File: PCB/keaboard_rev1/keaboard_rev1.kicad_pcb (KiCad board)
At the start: 2 copper layers, 136.5 x 87.7 mm, 100 parts, among them K01 KEYSW, K02 KEYSW, K03 KEYSW, K04 KEYSW, K05 KEYSW, K06 KEYSW, K07 KEYSW, K08 KEYSW, K09 KEYSW, K10 KEYSW, K11 KEYSW, K12 KEYSW, K13 KEYSW, K14 KEYSW, K15 KEYSW, K16 KEYSW, K17 KEYSW, K18 KEYSW, K19 KEYSW, K20 KEYSW, K21 KEYSW, K22 KEYSW, K23 KEYSW, K24 KEYSW, K25 KEYSW, U1 ProMicro

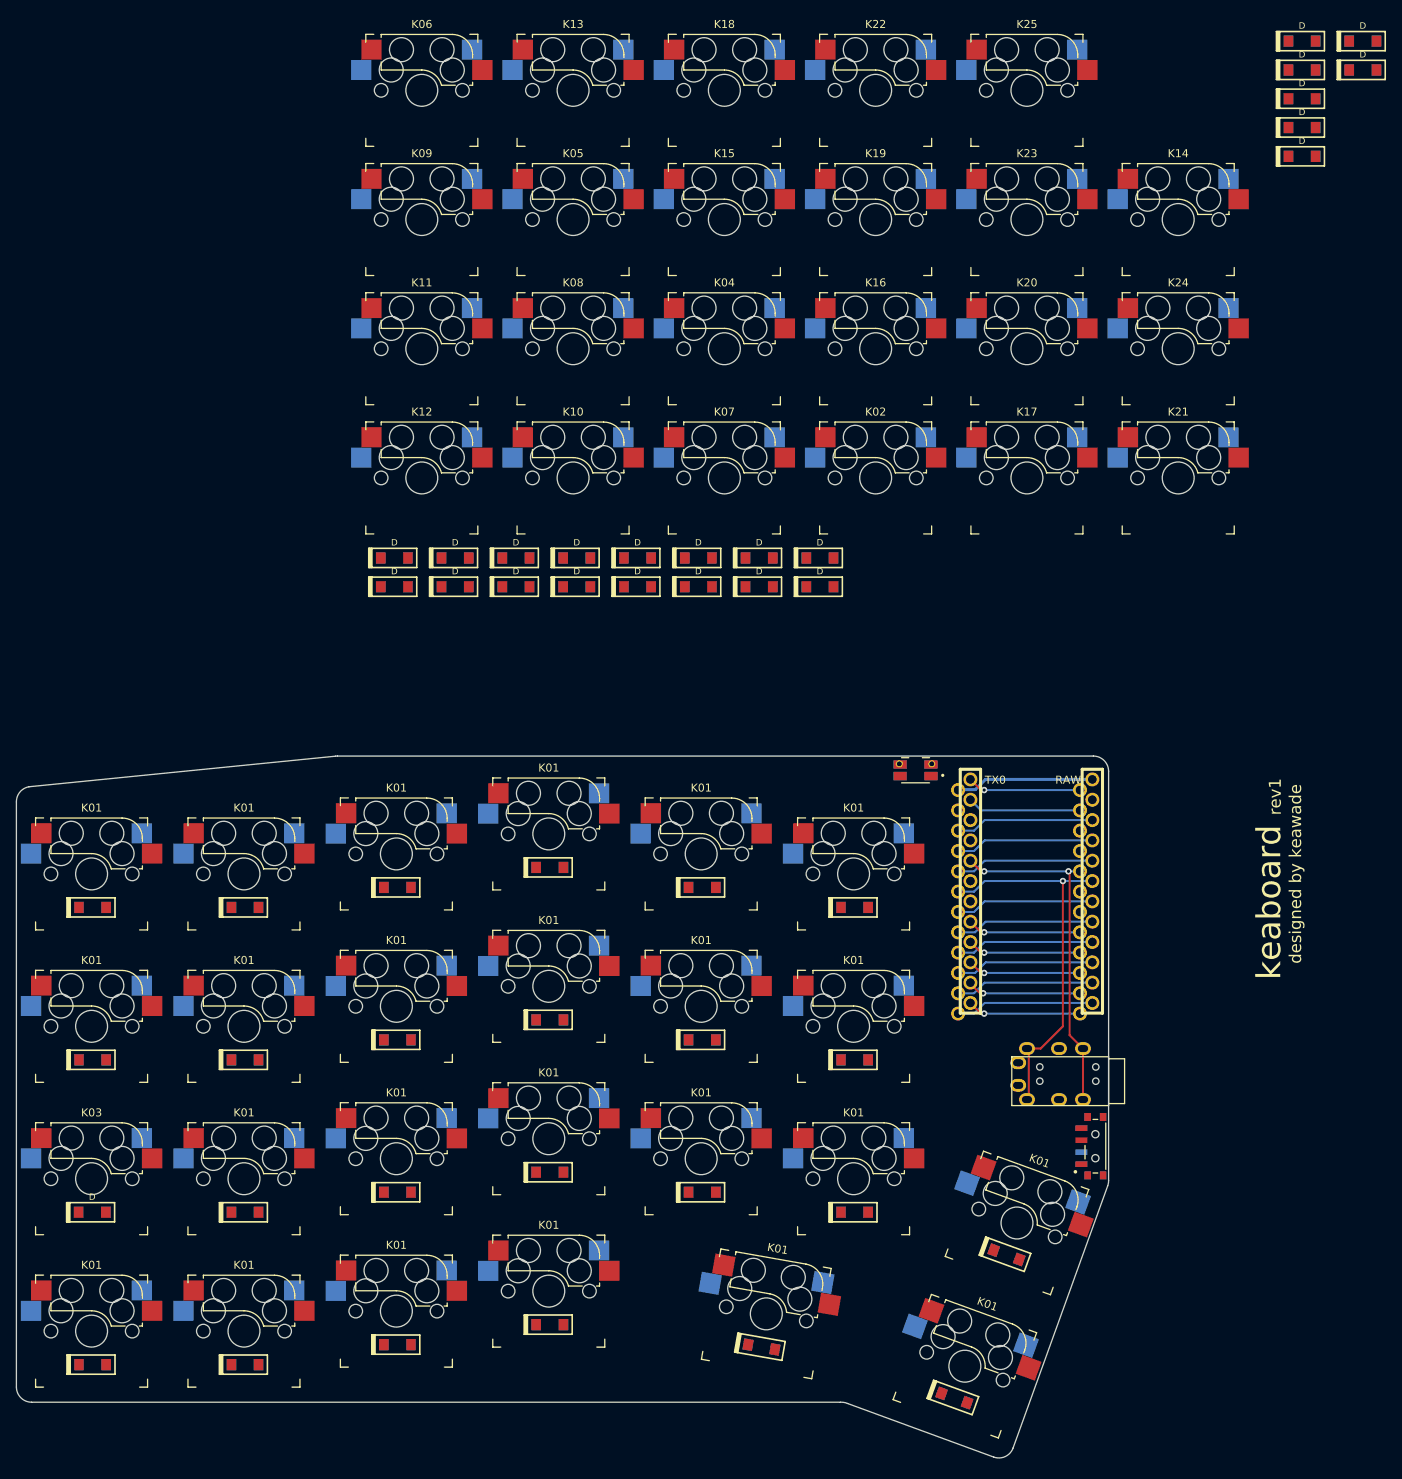
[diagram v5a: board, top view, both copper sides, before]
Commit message: Footprints laid out from schematic
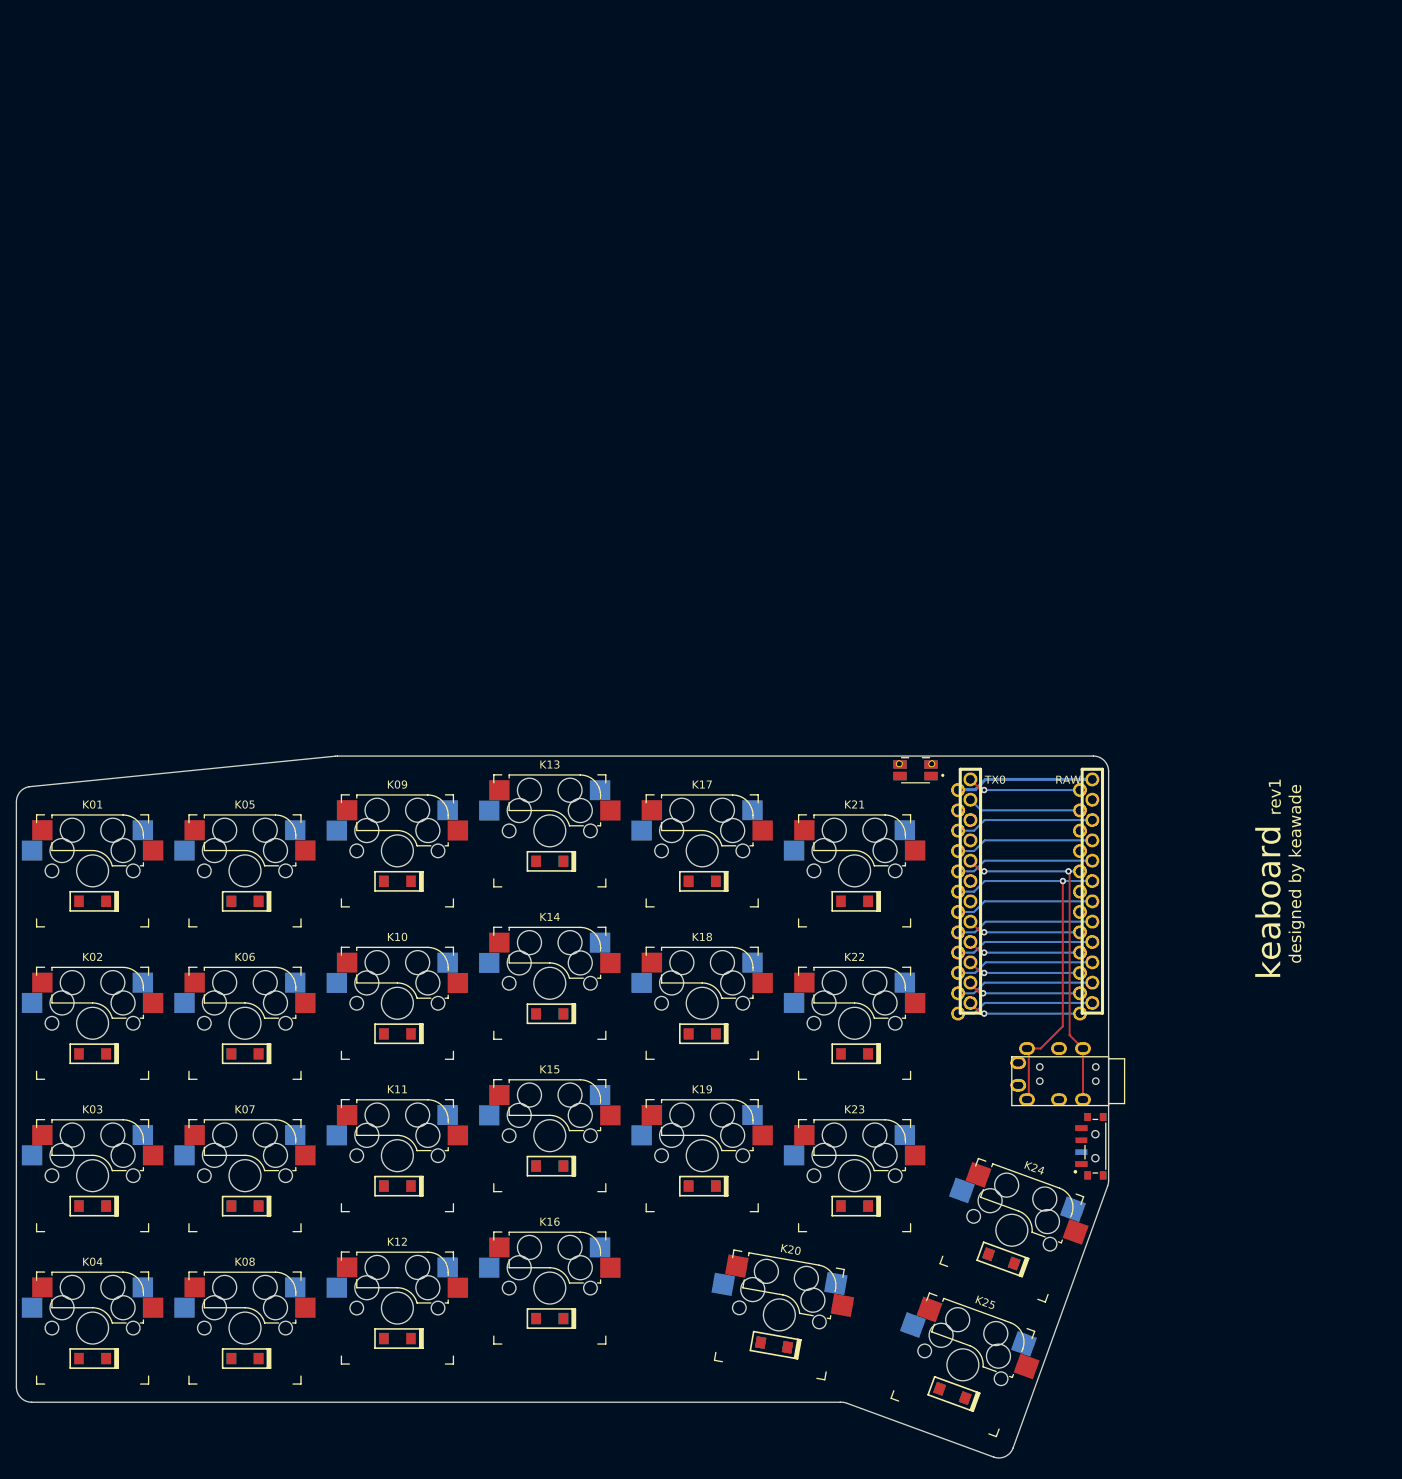
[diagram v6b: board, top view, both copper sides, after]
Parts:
- removed the D01 at (146.2, 107.9)
- removed the D01 at (95.6, 98.8)
- removed the D01 at (95.6, 79.7)
- removed the D01 at (95.6, 60.7)
- removed the D01 at (95.6, 41.6)
- removed the D01 at (76.6, 101.3)
- removed the D01 at (76.6, 82.2)
- removed the D01 at (76.6, 63.2)
- removed the D01 at (76.6, 44.1)
- removed the D01 at (57.5, 103.8)
- removed the D01 at (57.5, 84.7)
- removed the D01 at (152.7, 90.0)
- removed the D01 at (57.5, 65.7)
- removed the D01 at (57.5, 46.6)
- removed the D01 at (38.5, 103.8)
- removed the D01 at (38.5, 65.7)
- removed the D01 at (38.5, 46.6)
- removed the D01 at (122.1, 101.6)
- removed the D01 at (133.7, 84.7)
- removed the D01 at (133.7, 65.7)
- removed the D01 at (133.7, 46.6)
- removed the D01 at (114.7, 82.2)
- removed the D01 at (114.7, 63.2)
- removed the D01 at (114.7, 44.1)
- removed the K01 at (147.5, 104.0)
- removed the K01 at (95.5, 94.6)
- removed the K01 at (95.5, 75.5)
- removed the K01 at (95.5, 56.5)
- removed the K01 at (95.5, 37.4)
- removed the K01 at (76.5, 97.1)
- removed the K01 at (76.5, 78.0)
- removed the K01 at (76.5, 59.0)
- removed the K01 at (76.5, 39.9)
- removed the K01 at (57.4, 99.6)
- removed the K01 at (57.4, 80.5)
- removed the K01 at (154.0, 86.1)
- removed the K01 at (57.4, 61.5)
- removed the K01 at (57.4, 42.4)
- removed the K01 at (38.4, 99.6)
- removed the K01 at (38.4, 61.5)
- removed the K01 at (38.4, 42.4)
- removed the K01 at (122.7, 97.4)
- removed the K01 at (133.6, 80.5)
- removed the K01 at (133.6, 61.5)
- removed the K01 at (133.6, 42.4)
- removed the K01 at (114.6, 78.0)
- removed the K01 at (114.6, 59.0)
- removed the K01 at (114.6, 39.9)
- added D01: D, parts:D_SOD123_reversible, B.Cu at (38.5, 45.8)
- added K01: KEYSW, parts:Kailh_socket_MX_reversible, B.Cu at (38.5, 42.0)
- D02, D03, D04, D05, D06, D07, D08, D09, D10, D11, D12, D13, D14, D15, D16, D17, D18, D19, D20, D21, D22, D23, D24, D25: moved to B.Cu
- moved D04 226.2 mm to (38.5, 103.0)
- moved D12 197.7 mm to (76.6, 100.5)
- moved D06 178.1 mm to (57.5, 64.9)
- moved D10 173.1 mm to (76.6, 62.4)
- moved D05 163.7 mm to (57.5, 45.8)
- moved K25 159.5 mm to (147.3, 103.8), turned to 160 degrees
- moved D09 151.9 mm to (76.6, 43.3)
- moved K04 145.7 mm to (38.5, 99.2)
- moved D14 142.6 mm to (95.6, 59.9)
- moved K08 129.1 mm to (57.5, 99.2)
- moved K20 124.7 mm to (124.3, 97.5), turned to 170 degrees
- moved K16 124.3 mm to (95.6, 94.2)
- moved K14 123.6 mm to (95.6, 56.1)
- moved K23 121.4 mm to (133.7, 80.1)
- moved K02 119.3 mm to (38.5, 61.1)
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
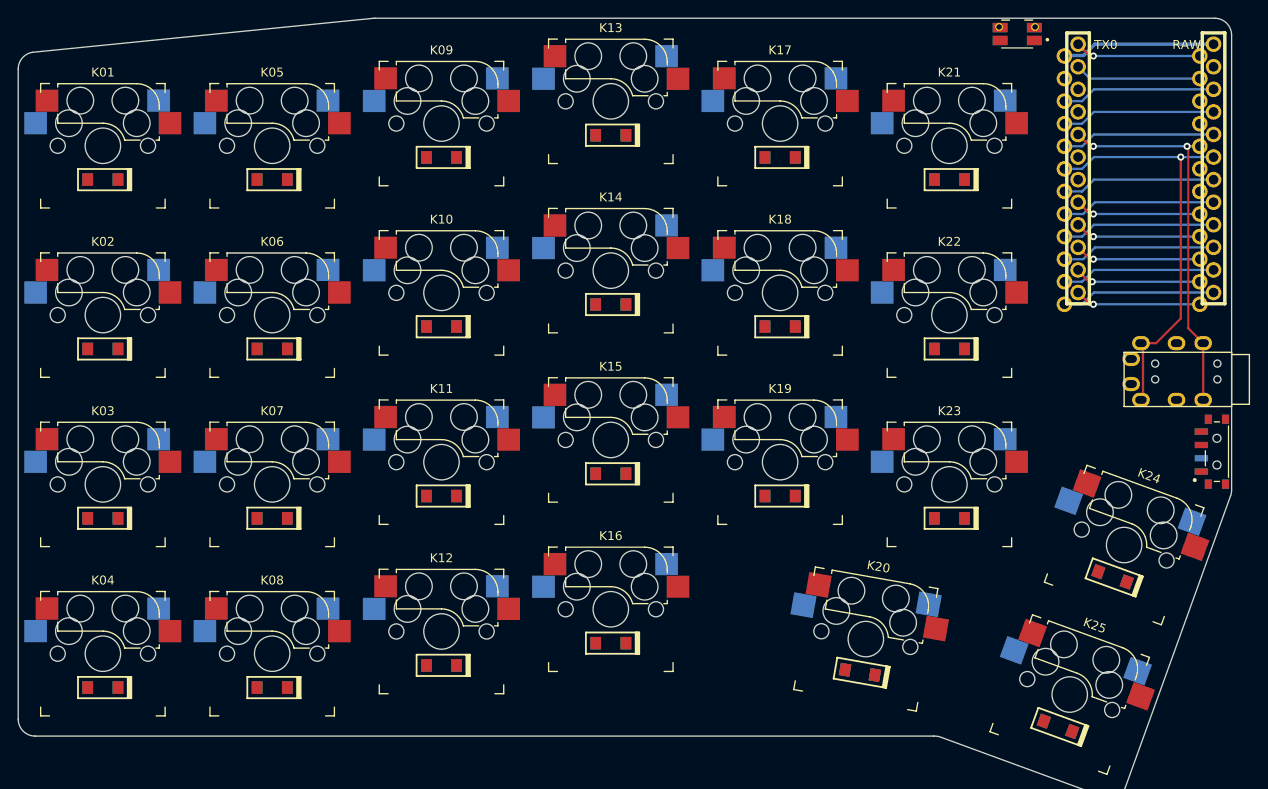
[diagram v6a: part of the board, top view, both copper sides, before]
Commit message: Wired matrix
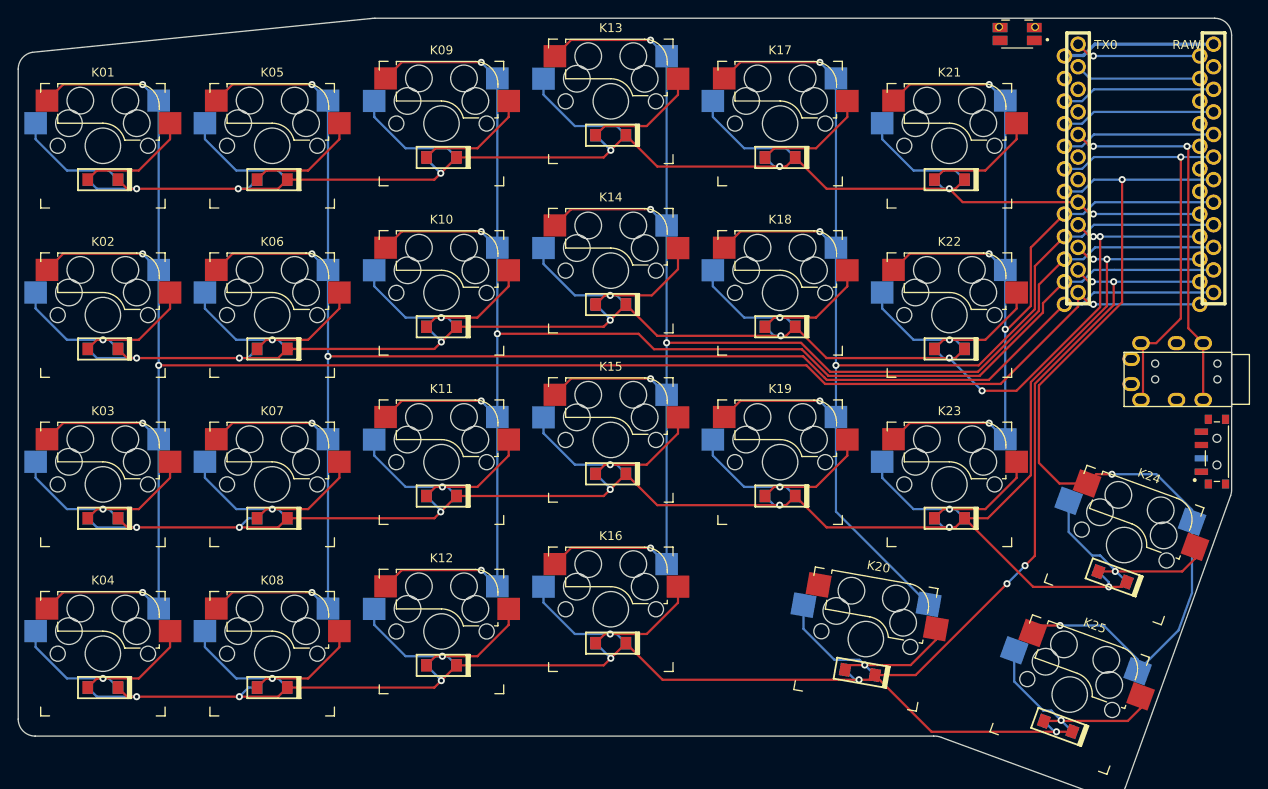
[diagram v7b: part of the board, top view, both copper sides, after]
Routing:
- net COL1: track 14.3 -> 237.2 mm, vias 1 -> 6
- net COL2: track 17.3 -> 218.2 mm, vias 0 -> 5
- net ROW4: track 14.3 -> 204.3 mm, vias 1 -> 10
- net COL3: track 17.3 -> 201.5 mm, vias 0 -> 5
- net ROW3: track 14.3 -> 194.8 mm, vias 1 -> 9
- net COL4: track 17.3 -> 183.8 mm, vias 0 -> 5
- net ROW2: track 14.3 -> 164.0 mm, vias 1 -> 9
- net COL5: track 17.3 -> 157.5 mm, vias 0 -> 4
- net ROW1: track 14.3 -> 148.8 mm, vias 1 -> 7
- net COL6: track 17.3 -> 113.5 mm, vias 0 -> 4
- net COL7: track 17.3 -> 108.8 mm, vias 0 -> 3
- net Net-(D14-Pad2): track 0.00 -> 26.2 mm, vias 0 -> 1
- net Net-(D11-Pad2): track 0.00 -> 25.9 mm, vias 0 -> 1
- net Net-(D23-Pad2): track 0.00 -> 25.9 mm, vias 0 -> 1
- net Net-(D19-Pad2): track 0.00 -> 25.9 mm, vias 0 -> 1
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
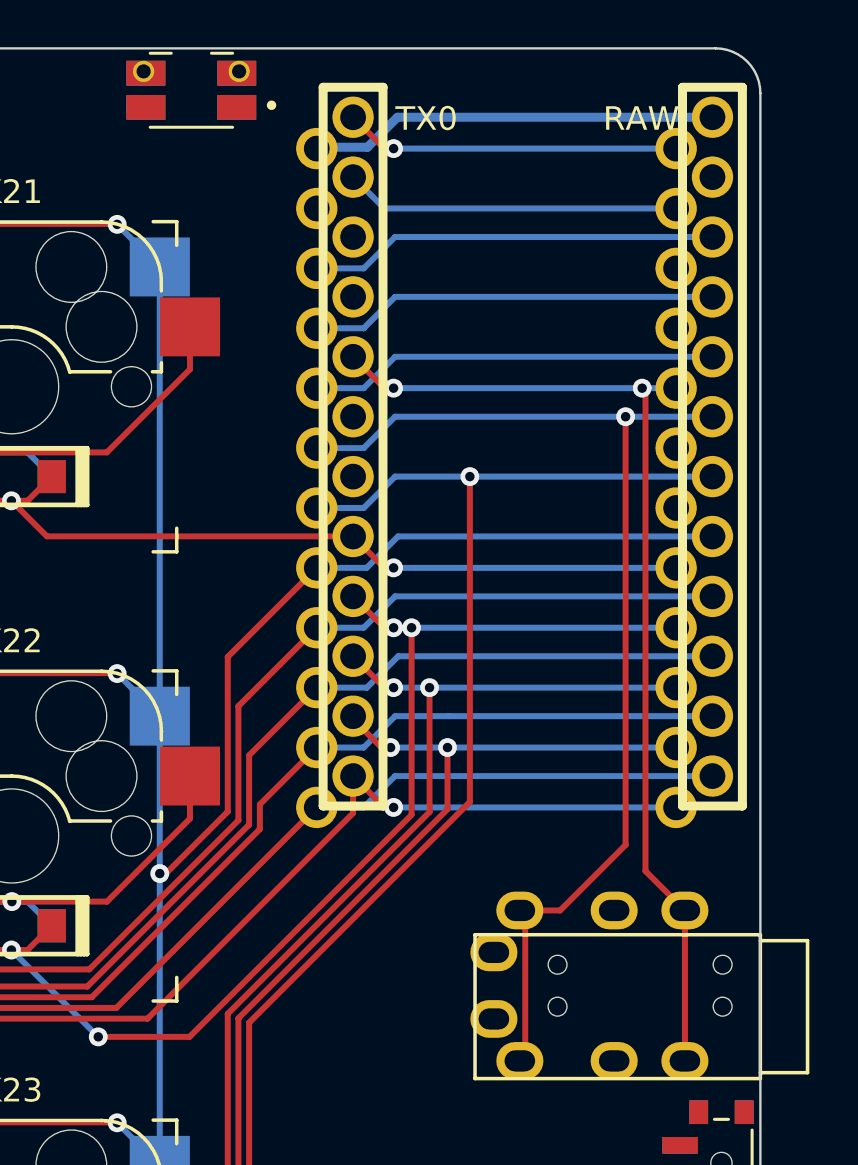
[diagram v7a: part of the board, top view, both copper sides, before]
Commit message: Fix reset switch, wire reset switch, wire grounds
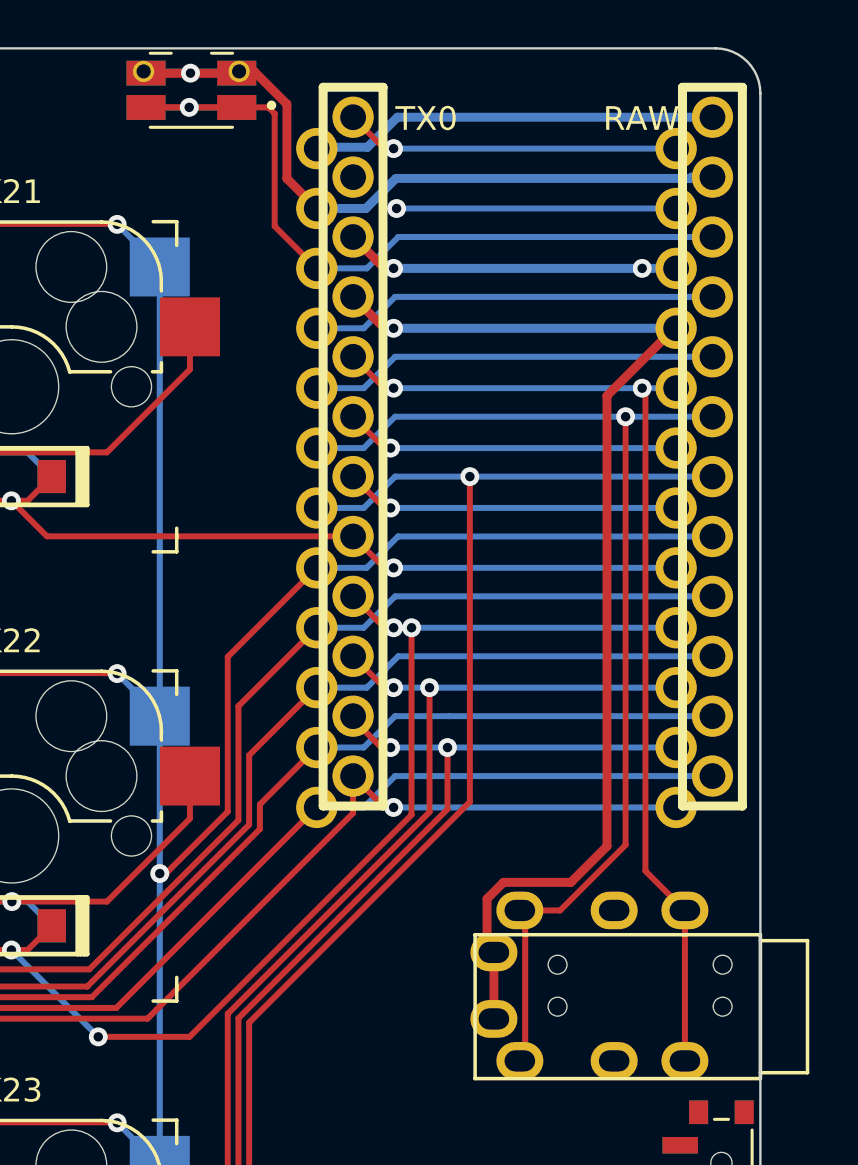
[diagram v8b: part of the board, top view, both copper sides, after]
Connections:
- U1 pad 22: RST -> RESET
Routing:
- net GND: track 0.00 -> 95.8 mm, vias 0 -> 4
- net RESET: track 0.00 -> 34.0 mm, vias 0 -> 1
- net RST: track 17.3 -> 0.00 mm
- net Net-(U1-Pad7): track 0.00 -> 14.3 mm, vias 0 -> 1
- net Net-(U1-Pad6): track 0.00 -> 14.3 mm, vias 0 -> 1
- net Net-(U1-Pad2): track 14.3 -> 11.9 mm, vias 0 -> 1
